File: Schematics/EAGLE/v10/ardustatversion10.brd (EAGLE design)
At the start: 68.2 x 57 mm, 29 parts

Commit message: Added switch and moved some wires
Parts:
- removed POT: (no value), ic-package:SOCKET-14
- added JP2, JP3: (no value), pinhead:1X03
- added JP4, JP5: (no value), pinhead:1X04
- added U$7: CD4066, ardustat:CD4066
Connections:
- new net N$23: JP3.1, JP3.3, RELAY.7
- new net N$28: JP4.2, U$7.P$3
- new net N$30: U$7.P$9
- new net N$31: JP4.4, U$7.P$10
- net GND: now also U$7.P$7; no longer POT.4
- net N$11: no longer ADCS.2, POT.8, RELAY.1
- net N$15: now also ADCS.2, U$7.P$1, U$7.P$11, U$7.P$4, U$7.P$8
- net N$2: no longer POT.2
- net N$22: now also U$7.P$14
- net N$26: no longer RELAY.7
- net N$27: now also JP4.1, U$7.P$2; no longer JP1.1, U$4.1456, U$4.5
- net N$29: no longer POT.14
- net N$3: no longer POT.3
- net N$8: now also JP5.1, JP5.2, JP5.3, JP5.4, RELAY.1; no longer POT.9
- net N$9: now also JP1.1, JP2.1, JP2.2, JP2.3, U$4.1456, U$4.5; no longer J1.8, POT.1

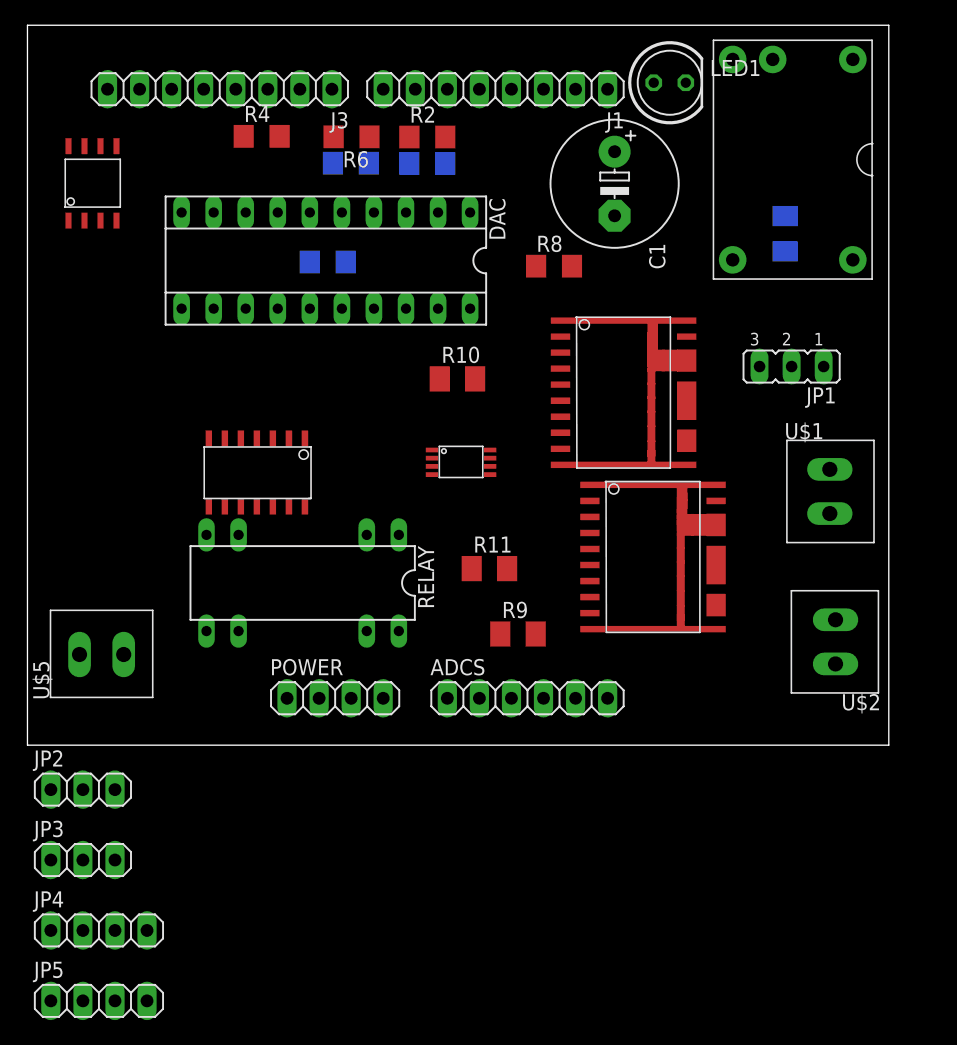
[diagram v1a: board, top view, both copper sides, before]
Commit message: Almost finished V10 board schematic
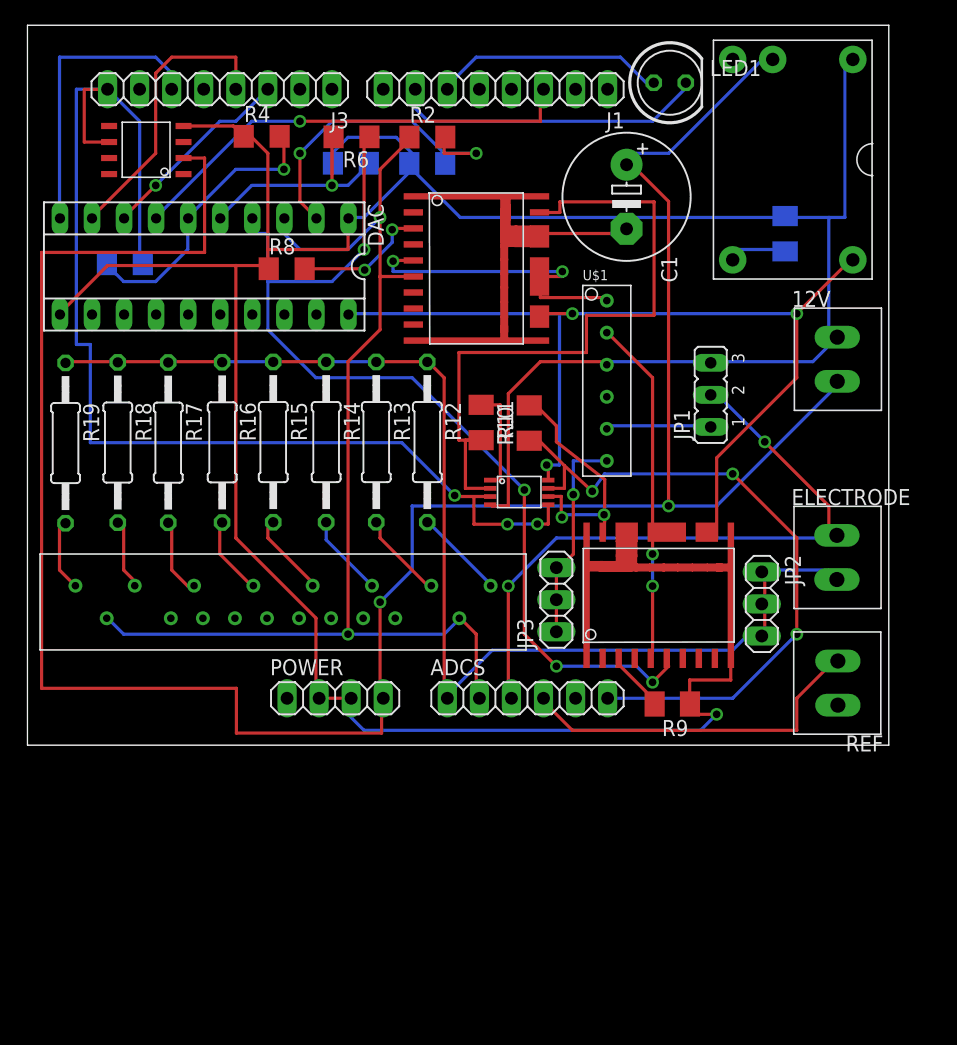
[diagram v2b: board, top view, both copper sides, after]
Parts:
- removed JP4, JP5: (no value), pinhead:1X04
- removed RELAY: (no value), ic-package:DIL14/8
- removed U$2, U$5: SPARK_SCREW_TERM, ardustat:SPARK_SCREW_TERM
- added 12V, ELECTRODE, REF: SPARK_SCREW_TERM, ardustat:SPARK_SCREW_TERM
- added R12, R13, R14, R15, R16, R17, R18, R19: (no value), resistor:0207/12
- R1, R2, R5, R6: value (none) -> 10k
- R10, R11: value (none) -> 1187
- R3, R4: value (none) -> 1k
- R7: value (none) -> 41.2
- R8, R9: value (none) -> 5.76k
- U$1: value SPARK_SCREW_TERM -> MS05-2A87; device ardustat:SPARK_SCREW_TERM -> ardustat:MS05-2A87
- U$7: value CD4066 -> RM05-8A; device ardustat:CD4066 -> ardustat:RM05-8A
- moved JP2 55.8 mm to (58.2, 25.3), turned to 270 degrees
- moved JP3 42.8 mm to (41.9, 25.6), turned to 90 degrees
- moved U$3 26.8 mm to (35.6, 51.9)
- moved R8 21.2 mm to (20.5, 51.8)
- moved U$1 19.7 mm to (45.9, 42.9)
- moved U$4 16.4 mm to (49.9, 25.9), turned to 90 degrees
- moved R3 16.1 mm to (7.72, 52.2)
- moved R9 13.4 mm to (51.1, 17.3), turned to 180 degrees
- moved R11 12.0 mm to (39.8, 39.6), turned to 90 degrees
- moved U$7 10.5 mm to (20.3, 25.4), turned to 90 degrees
- moved DAC 9.65 mm to (14.0, 52.0)
- moved JP1 6.79 mm to (54.1, 41.8), turned to 90 degrees
- moved TRANS-AMP 5.19 mm to (38.9, 34.1)
- moved U$6 4.93 mm to (9.35, 61.2), turned to 180 degrees
- moved R10 3.93 mm to (35.9, 39.6), turned to 270 degrees
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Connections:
- removed net N$29: DAC.20, POWER.1, R3.2
- new net N$33: R17.2, U$7.P$16
- new net N$34: R18.2, U$7.P$17
- new net N$35: R19.2, U$7.P$18
- new net N$36: JP1.1, U$1.P$5
- net GND: now also 12V.2, U$1.P$3; no longer RELAY.2, U$5.2, U$7.P$7
- net N$11: now also R12.2, U$7.P$11; no longer TRANS-AMP.5
- net N$15: now also U$7.P$10; no longer U$7.P$11, U$7.P$4, U$7.P$8
- net N$19: now also DAC.20
- net N$20: now also REF.1; no longer U$2.1
- net N$21: now also ELECTRODE.2; no longer TRANS-AMP.3, U$1.2
- net N$22: now also 12V.1; no longer U$5.1, U$7.P$14
- net N$23: now also JP3.2, U$1.P$6; no longer RELAY.7
- net N$24: now also R3.2, TRANS-AMP.3, TRANS-AMP.5
- net N$26: now also U$1.P$1
- net N$27: now also R13.2, U$7.P$12; no longer JP4.1, U$7.P$2
- net N$28: now also R14.2, U$7.P$13; no longer JP4.2, U$7.P$3
- net N$30: now also R15.2, U$7.P$14; no longer U$7.P$9
- net N$31: now also R16.2, U$7.P$15; no longer JP4.4, U$7.P$10
- net N$6: no longer RELAY.6
- net N$8: now also ELECTRODE.1, JP2.1, JP2.2, JP2.3, R12.1, R13.1, R14.1, R15.1, R16.1, R17.1, R18.1, R19.1; no longer JP5.1, JP5.2, JP5.3, JP5.4, RELAY.1, U$1.1
- net N$9: now also U$1.P$2; no longer JP1.1, JP2.1, JP2.2, JP2.3
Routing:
- net GND: track 0.00 -> 241.0 mm, vias 0 -> 1
- net N$22: track 0.00 -> 189.4 mm, vias 0 -> 2
- net N$8: track 0.00 -> 100.5 mm
- net N$24: track 0.00 -> 98.0 mm, vias 0 -> 3
- net N$15: track 0.00 -> 91.1 mm, vias 0 -> 2
- net N$19: track 0.00 -> 80.2 mm, vias 0 -> 3
- net N$32: track 0.00 -> 79.3 mm, vias 0 -> 4
- net N$48: track 0.00 -> 53.6 mm, vias 0 -> 3
- net N$10: track 0.00 -> 53.1 mm
- net N$21: track 0.00 -> 53.1 mm, vias 0 -> 2
- net N$5: track 0.00 -> 36.3 mm, vias 0 -> 1
- net N$9: track 0.00 -> 29.2 mm, vias 0 -> 2
- net N$20: track 0.00 -> 28.6 mm
- net N$7: track 0.00 -> 26.5 mm, vias 0 -> 2
- net N$26: track 0.00 -> 25.2 mm, vias 0 -> 2
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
